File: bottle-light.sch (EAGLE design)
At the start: 66 parts, among them IC1 STM32F334K8T, IC2 LF33, T1 BC337, T2 BC337, T3 BC337, X1 1725656

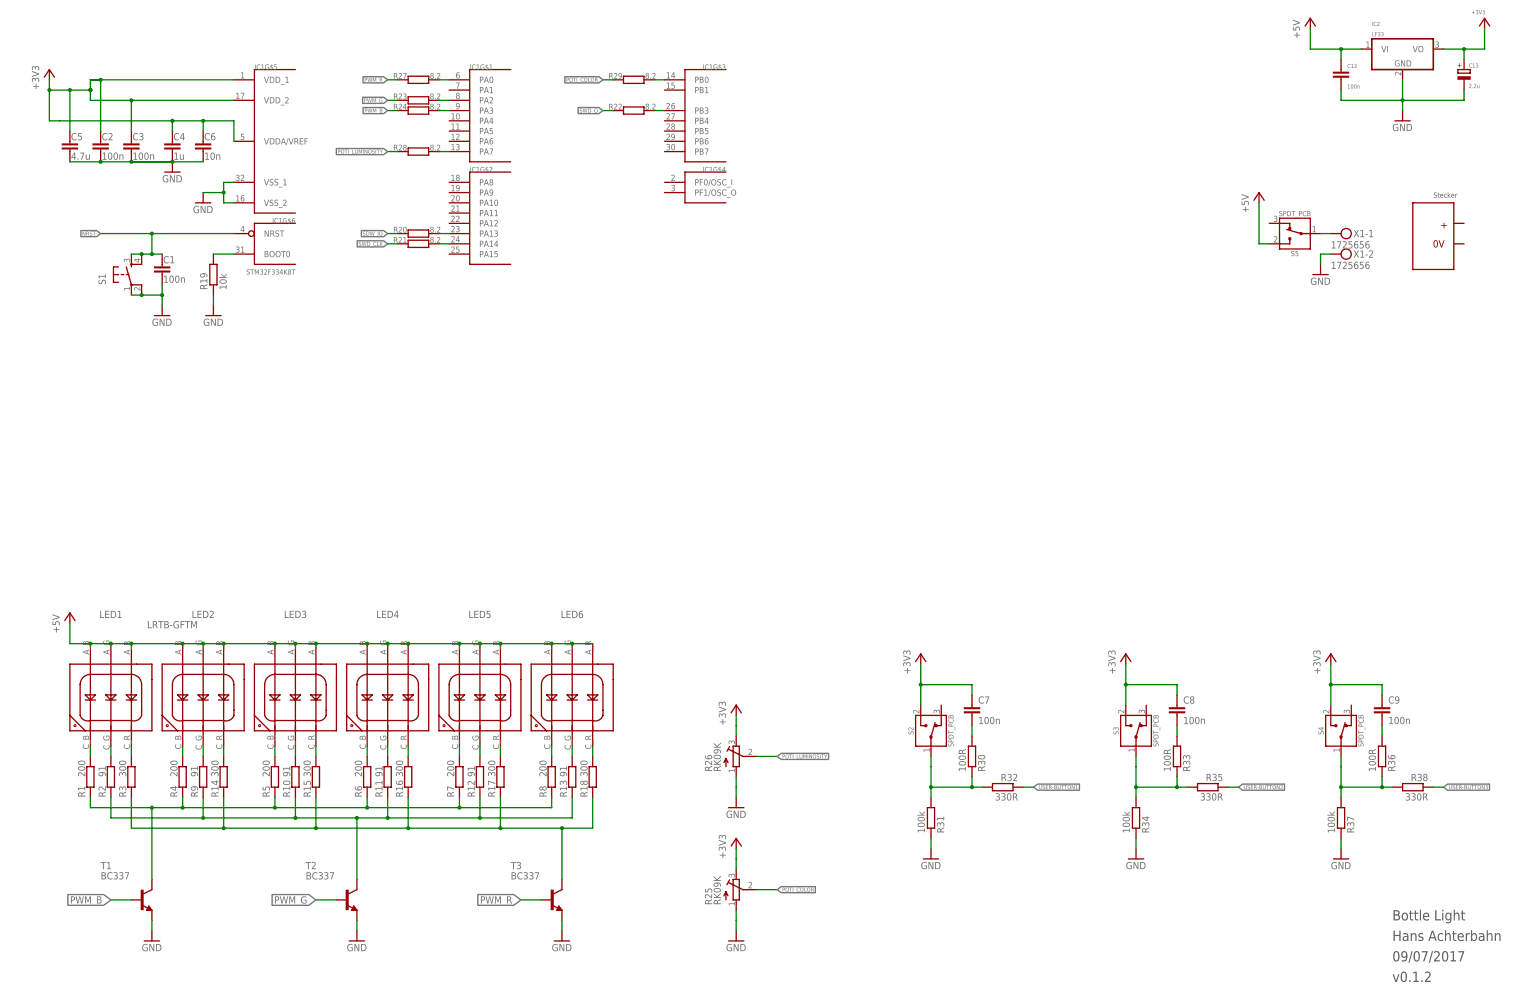
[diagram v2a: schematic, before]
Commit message: v0.1.3 schematic finished and board is routed - added new buttons - added swd debugger port - added battery pack - changed stm32 pinning - changed dc power supply port - removed reset button - added base resistors to transistors - routed board
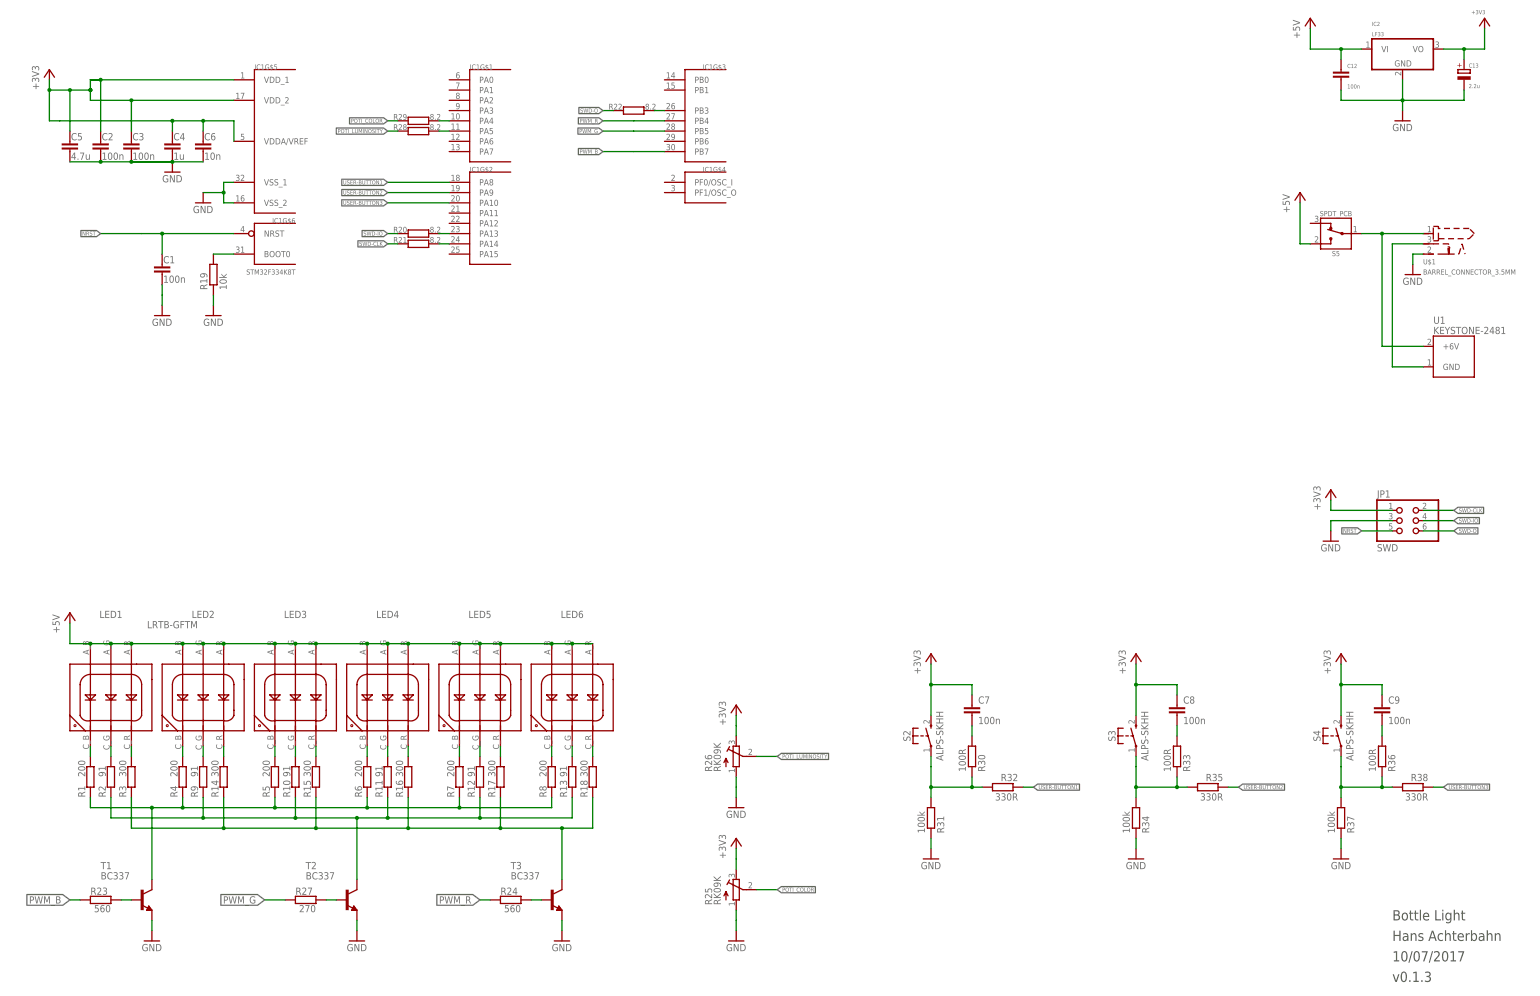
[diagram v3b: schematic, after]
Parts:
- removed S1: (no value), h8-switch:TAC_SWITCHPTH
- removed X1: 1725656, con-phoenix-508:MKDSN1,5/2-5,08
- added JP1: SWD, h8-pinhead:PINHD-2X3_2.54-SMD
- added U$1: BARREL_CONNECTOR_3.5MM, h8-conector:BARREL_CONNECTOR_3.5MM
- added U1: KEYSTONE-2481, h8-misc:KEYSTONE-2481
- R23, R24: value 8.2 -> 560; RS-ONLINE 904-5027 -> 631-6339
- R27: value 8.2 -> 270; RS-ONLINE 904-5027 -> 631-6250
- S2, S3, S4: value SPDT_PCB -> ALPS-SKHH; device h8-switch:SPDT_PCB -> h8-switch:ALPS-SKHH
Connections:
- removed net N$37: S5.1, X1-1.KL
- removed net SDW_IO: R20.1
- removed net SWD_CLK: R21.1
- removed net SWD_O: R22.1
- new net +6V: S5.1, U$1.1, U1.+6V
- new net SWD-CLK: JP1.2, R21.1
- new net SWD-IO: JP1.4, R20.1
- new net SWD-O: JP1.6, R22.1
- net +3V3: now also JP1.1
- net GND: now also JP1.3, U$1.2, U$1.3, U1.GND; no longer S1.1, S1.2, X1-2.KL
- net N$26: now also R23.2, T1.B; no longer IC1G$1.PA0, R27.2
- net N$27: now also R24.2, T3.B; no longer IC1G$1.PA2, R23.2
- net N$28: now also R27.2, T2.B; no longer IC1G$1.PA3, R24.2
- net N$29: now also IC1G$1.PA4, R29.2; no longer IC1G$1.PA7, R28.2
- net N$34: now also IC1G$1.PA5, R28.2; no longer IC1G$3.PB0, R29.2
- net NRST: now also JP1.5; no longer S1.3, S1.4
- net PWM_B: now also IC1G$3.PB7, R23.1; no longer R24.1, T1.B
- net PWM_G: now also IC1G$3.PB5, R27.1; no longer R23.1, T2.B
- net PWM_R: now also IC1G$3.PB4, R24.1; no longer R27.1, T3.B
- net USER-BUTTON1: now also IC1G$2.PA8
- net USER-BUTTON2: now also IC1G$2.PA9
- net USER-BUTTON3: now also IC1G$2.PA10
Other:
- note added: "10/07/2017"
- note added: "v0.1.3"
- note removed: "09/07/2017"
- note removed: "Stecker"
- note removed: "v0.1.2"
- moved on the sheet: R23, R24, R27, R28, R29, S5

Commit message: v0.2.0 Neue LEDs hinzugefügt: APA102
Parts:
- added LD1, LD10, LD11, LD12, LD13, LD14, LD15, LD16, LD17, LD18, LD19, LD2, LD20, LD3, LD4, LD5, LD6, LD7, LD8, LD9: APA102, 3587:APA102APA102C-5050
- added X1: MINI-USB-SHIELD-UX60A-MB-5ST, con-hirose:MINI-USB-SHIELD-UX60A-MB-5ST
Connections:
- new net N$37: LD1.CKO, LD2.CKI
- new net N$39: LD1.SDO, LD2.SDI
- new net N$40: LD2.CKO, LD3.CKI
- new net N$41: LD2.SDO, LD3.SDI
- new net N$42: LD3.CKO, LD4.CKI
- new net N$43: LD3.SDO, LD4.SDI
- new net N$44: LD4.CKO, LD5.CKI
- new net N$45: LD4.SDO, LD5.SDI
- new net N$46: LD5.CKO, LD6.CKI
- new net N$47: LD5.SDO, LD6.SDI
- new net N$48: LD6.CKO, LD7.CKI
- new net N$49: LD6.SDO, LD7.SDI
- new net N$50: LD7.CKO, LD8.CKI
- new net N$51: LD7.SDO, LD8.SDI
- new net N$52: LD8.CKO, LD9.CKI
- new net N$53: LD8.SDO, LD9.SDI
- new net N$54: LD10.CKI, LD9.CKO
- new net N$55: LD10.SDI, LD9.SDO
- new net N$56: LD10.CKO, LD11.CKI
- new net N$57: LD10.SDO, LD11.SDI
- new net N$58: LD11.CKO, LD12.CKI
- new net N$59: LD11.SDO, LD12.SDI
- new net N$60: LD12.CKO, LD13.CKI
- new net N$61: LD12.SDO, LD13.SDI
- new net N$62: LD13.CKO, LD14.CKI
- new net N$63: LD13.SDO, LD14.SDI
- new net N$64: LD14.CKO, LD15.CKI
- new net N$65: LD14.SDO, LD15.SDI
- new net N$66: LD15.CKO, LD16.CKI
- new net N$67: LD15.SDO, LD16.SDI
- new net N$68: LD16.CKO, LD17.CKI
- new net N$69: LD16.SDO, LD17.SDI
- new net N$70: LD17.CKO, LD18.CKI
- new net N$71: LD17.SDO, LD18.SDI
- new net N$72: LD18.CKO, LD19.CKI
- new net N$73: LD18.SDO, LD19.SDI
- new net N$74: LD19.CKO, LD20.CKI
- new net N$75: LD19.SDO, LD20.SDI
- new net N$76: LD1.CKI
- new net N$77: LD1.SDI
- net +5V: now also LD1.VDD, LD10.VDD, LD11.VDD, LD12.VDD, LD13.VDD, LD14.VDD, LD15.VDD, LD16.VDD, LD17.VDD, LD18.VDD, LD19.VDD, LD2.VDD, LD20.VDD, LD3.VDD, LD4.VDD, LD5.VDD, LD6.VDD, LD7.VDD, LD8.VDD, LD9.VDD
- net GND: now also LD1.GND, LD10.GND, LD11.GND, LD12.GND, LD13.GND, LD14.GND, LD15.GND, LD16.GND, LD17.GND, LD18.GND, LD19.GND, LD2.GND, LD20.GND, LD3.GND, LD4.GND, LD5.GND, LD6.GND, LD7.GND, LD8.GND, LD9.GND
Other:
- note removed: "10/07/2017"
- note removed: "Bottle Light"
- note removed: "Hans Achterbahn"
- note removed: "v0.1.3"
- moved on the sheet: LED1, LED2, LED3, LED4, LED5, LED6, R1, R10, R11, R12, R13, R14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

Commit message: v0.2.1 Die neuen LEDs positioniert
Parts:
- removed LD17, LD18, LD19, LD20: APA102, 3587:APA102APA102C-5050
- removed LED1, LED2, LED3, LED4, LED5, LED6: LRTB-GFTM, h8-optic:OSRAM_RGB-LED_LRTB-GFTM
- removed R10, R11, R12, R13, R9: 91, resistor:R-EU_R0603
- removed R14, R15, R16, R17, R18, R3: 300, resistor:R-EU_R0603
- removed R23, R24: 560, resistor:R-EU_R0603
- removed R27: 270, resistor:R-EU_R0603
- removed R4, R5, R6, R7, R8: 200, resistor:R-EU_R0603
- removed T1, T2, T3: BC337, transistor:BC337
- removed U1: KEYSTONE-2481, h8-misc:KEYSTONE-2481
- R1: value 200 -> 8.2; RS-ONLINE 678-9960 -> 904-5027
- R2: value 91 -> 8.2; RS-ONLINE 828-0942 -> 904-5027
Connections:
- removed net +6V: S5.1, U$1.1, U1.+6V
- removed net N$10: LED2.C_RED, R14.2
- removed net N$11: LED3.C_BLUE, R5.2
- removed net N$12: LED3.C_GREEN, R10.2
- removed net N$13: LED3.C_RED, R15.2
- removed net N$14: LED4.C_BLUE, R6.2
- removed net N$15: LED4.C_GREEN, R11.2
- removed net N$16: LED4.C_RED, R16.2
- removed net N$17: LED5.C_BLUE, R7.2
- removed net N$18: LED5.C_GREEN, R12.2
- removed net N$19: LED5.C_RED, R17.2
- removed net N$20: LED6.C_BLUE, R8.2
- removed net N$21: LED6.C_GREEN, R13.2
- removed net N$22: LED6.C_RED, R18.2
- removed net N$26: R23.2, T1.B
- removed net N$27: R24.2, T3.B
- removed net N$28: R27.2, T2.B
- removed net N$4: R14.1, R15.1, R16.1, R17.1, R18.1, R3.1, T3.C
- removed net N$5: LED1.C_BLUE, R1.2
- removed net N$6: LED1.C_GREEN, R2.2
- removed net N$68: LD16.CKO, LD17.CKI
- removed net N$69: LD16.SDO, LD17.SDI
- removed net N$7: LED1.C_RED, R3.2
- removed net N$70: LD17.CKO, LD18.CKI
- removed net N$71: LD17.SDO, LD18.SDI
- removed net N$72: LD18.CKO, LD19.CKI
- removed net N$73: LD18.SDO, LD19.SDI
- removed net N$74: LD19.CKO, LD20.CKI
- removed net N$75: LD19.SDO, LD20.SDI
- removed net N$77: LD1.SDI
- removed net N$8: LED2.C_BLUE, R4.2
- removed net N$9: LED2.C_GREEN, R9.2
- removed net PWM_B: IC1G$3.PB7, R23.1
- removed net PWM_G: IC1G$3.PB5, R27.1
- removed net PWM_R: IC1G$3.PB4, R24.1
- new net SPI-CLK: LD1.CKI, R1.1
- new net SPI-MOSI: LD1.SDI, R2.1
- net +5V: no longer LD17.VDD, LD18.VDD, LD19.VDD, LD20.VDD, LED1.A_BLUE, LED1.A_GREEN, LED1.A_RED, LED2.A_BLUE, LED2.A_GREEN, LED2.A_RED, LED3.A_BLUE, LED3.A_GREEN, LED3.A_RED, LED4.A_BLUE, LED4.A_GREEN, LED4.A_RED, LED5.A_BLUE, LED5.A_GREEN, LED5.A_RED, LED6.A_BLUE, LED6.A_GREEN, LED6.A_RED
- net GND: no longer LD17.GND, LD18.GND, LD19.GND, LD20.GND, T1.E, T2.E, T3.E, U$1.3, U1.GND
- net N$2: now also IC1G$1.PA5, R1.2; no longer R1.1, R4.1, R5.1, R6.1, R7.1, R8.1, T1.C
- net N$29: now also IC1G$1.PA0; no longer IC1G$1.PA4
- net N$3: now also IC1G$1.PA7, R2.2; no longer R10.1, R11.1, R12.1, R13.1, R2.1, R9.1, T2.C
- net N$34: now also IC1G$1.PA1; no longer IC1G$1.PA5
- net N$76: now also S5.1, U$1.1; no longer LD1.CKI
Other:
- moved on the sheet: C12, C13, IC2, LD1, LD10, LD11, LD12, LD13, LD14, LD15, LD16, LD2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
